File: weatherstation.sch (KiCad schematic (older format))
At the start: 29 parts, among them J1 Conn_02x13_Odd_Even, J10 Conn_01x03_Male, J2 Conn_01x02_Male, J3 Conn_01x02_Male, J4 Conn_01x02_Male, J5 Conn_01x02_Male, J6 Conn_01x02_Male, J7 Conn_01x02_Male, J8 Conn_01x02_Male, J9 Conn_01x02_Male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

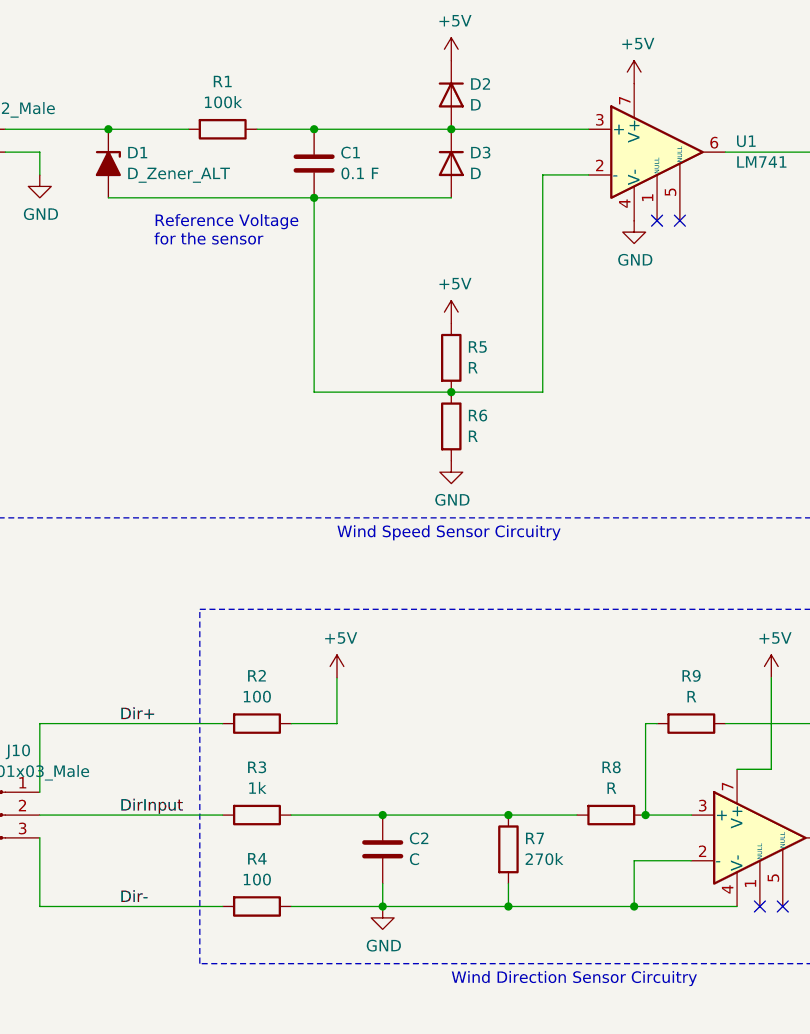
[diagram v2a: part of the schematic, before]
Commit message: Added footprints to schematic and generated netlist
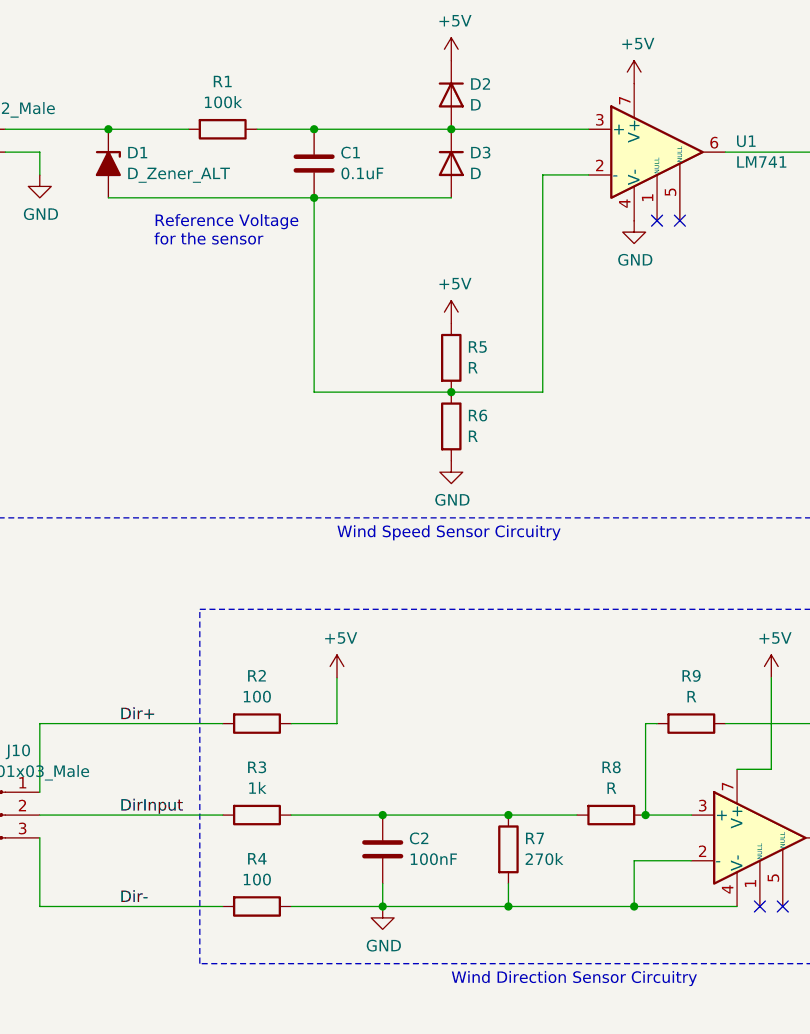
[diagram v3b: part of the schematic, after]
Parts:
- C1: value 0.1 F -> 0.1uF; footprint (none) -> Capacitor_THT:CP_Radial_D5.0mm_P2.50mm
- C2: value C -> 100nF; footprint (none) -> Capacitor_THT:C_Rect_L4.0mm_W2.5mm_P2.50mm
- D1, D2, D3: footprint (none) -> Diode_THT:D_A-405_P7.62mm_Horizontal
- D4: footprint (none) -> LED_THT:LED_D5.0mm
- J1: footprint (none) -> Connector_PinHeader_2.54mm:PinHeader_2x13_P2.54mm_Vertical
- J10: footprint (none) -> Connector_PinHeader_2.54mm:PinHeader_1x03_P2.54mm_Vertical
- J2, J3, J4, J5, J6, J7, J8, J9: footprint (none) -> Connector_PinHeader_2.54mm:PinHeader_1x02_P2.54mm_Vertical
- R1, R10, R2, R3, R4, R5, R6, R7, R8, R9: footprint (none) -> Resistor_THT:R_Axial_DIN0207_L6.3mm_D2.5mm_P10.16mm_Horizontal
- U1, U2: footprint (none) -> Package_DIP:DIP-8_W7.62mm
- U3: footprint (none) -> Package_DIP:DIP-16_W7.62mm
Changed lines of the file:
@@
 $EndDescr
-$Comp
-L Device:C C1
-U 1 1 60C0C43B
-P 2450 1350
-F 0 "C1" H 2565 1396 50  0000 L CNN
-F 1 "0.1 F" H 2565 1305 50  0000 L CNN
-F 2 "" H 2488 1200 50  0001 C CNN
-F 3 "~" H 2450 1350 50  0001 C CNN
-	1    2450 1350
-	1    0    0    -1
-$EndComp
-$Comp
-L Device:R R1
-U 1 1 60C0D3DD
-P 2050 1200
-F 0 "R1" V 1843 1200 50  0000 C CNN
-F 1 "100k" V 1934 1200 50  0000 C CNN
-F 2 "" V 1980 1200 50  0001 C CNN
-F 3 "~" H 2050 1200 50  0001 C CNN
-	1    2050 1200
-	0    1    1    0
-$EndComp
-Wire Wire Line
-	2200 1200 2450 1200
 $Comp
 L Device:D_Zener_ALT D1
@@
 F 0 "D1" V 1504 1430 50  0000 L CNN
 F 1 "D_Zener_ALT" V 1595 1430 50  0000 L CNN
-F 2 "" H 1550 1350 50  0001 C CNN
+F 2 "Diode_THT:D_A-405_P7.62mm_Horizontal" H 1550 1350 50  0001 C CNN
 F 3 "~" H 1550 1350 50  0001 C CNN
 	1    1550 1350
 	0    1    1    0
 $EndComp
-Wire Wire Line
-	1900 1200 1550 1200
 $Comp
 L Device:D D3
@@
 F 0 "D3" V 3004 1430 50  0000 L CNN
 F 1 "D" V 3095 1430 50  0000 L CNN
-F 2 "" H 3050 1350 50  0001 C CNN
+F 2 "Diode_THT:D_A-405_P7.62mm_Horizontal" H 3050 1350 50  0001 C CNN
 F 3 "~" H 3050 1350 50  0001 C CNN
 	1    3050 1350
@@
 F 0 "D2" V 3004 1130 50  0000 L CNN
 F 1 "D" V 3095 1130 50  0000 L CNN
-F 2 "" H 3050 1050 50  0001 C CNN
+F 2 "Diode_THT:D_A-405_P7.62mm_Horizontal" H 3050 1050 50  0001 C CNN
 F 3 "~" H 3050 1050 50  0001 C CNN
 	1    3050 1050
 	0    1    1    0
 $EndComp
-Wire Wire Line
-	2450 1200 3050 1200
-Connection ~ 2450 1200
 Connection ~ 3050 1200
 $Comp
@@
 F 0 "U1" H 4294 1346 50  0000 L CNN
 F 1 "LM741" H 4294 1255 50  0000 L CNN
-F 2 "" H 4000 1350 50  0001 C CNN
+F 2 "Package_DIP:DIP-8_W7.62mm" H 4000 1350 50  0001 C CNN
 F 3 "http://www.ti.com/lit/ds/symlink/lm741.pdf" H 4100 1450 50  0001 C CNN
 	1    3950 1300
@@
 F 0 "R5" H 3120 2246 50  0000 L CNN
 F 1 "R" H 3120 2155 50  0000 L CNN
-F 2 "" V 2980 2200 50  0001 C CNN
+F 2 "Resistor_THT:R_Axial_DIN0207_L6.3mm_D2.5mm_P10.16mm_Horizontal" V 2980 2200 50  0001 C CNN
 F 3 "~" H 3050 2200 50  0001 C CNN
 	1    3050 2200
@@
 F 0 "R6" H 3120 2546 50  0000 L CNN
 F 1 "R" H 3120 2455 50  0000 L CNN
-F 2 "" V 2980 2500 50  0001 C CNN
+F 2 "Resistor_THT:R_Axial_DIN0207_L6.3mm_D2.5mm_P10.16mm_Horizontal" V 2980 2500 50  0001 C CNN
 F 3 "~" H 3050 2500 50  0001 C CNN
 	1    3050 2500
@@
 F 0 "R10" H 4770 1496 50  0000 L CNN
 F 1 "R" H 4770 1405 50  0000 L CNN
-F 2 "" V 4630 1450 50  0001 C CNN
+F 2 "Resistor_THT:R_Axial_DIN0207_L6.3mm_D2.5mm_P10.16mm_Horizontal" V 4630 1450 50  0001 C CNN
 F 3 "~" H 4700 1450 50  0001 C CNN
 	1    4700 1450
@@
 F 0 "D4" V 4739 1632 50  0000 R CNN
 F 1 "LED" V 4648 1632 50  0000 R CNN
-F 2 "" H 4700 1750 50  0001 C CNN
+F 2 "LED_THT:LED_D5.0mm" H 4700 1750 50  0001 C CNN
 F 3 "~" H 4700 1750 50  0001 C CNN
 	1    4700 1750
@@
 F 0 "U3" H 6550 2431 50  0000 C CNN
 F 1 "MCP3008" H 6550 2340 50  0000 C CNN
-F 2 "" H 6650 1850 50  0001 C CNN
+F 2 "Package_DIP:DIP-16_W7.62mm" H 6650 1850 50  0001 C CNN
 F 3 "http://ww1.microchip.com/downloads/en/DeviceDoc/21295d.pdf" H 6650 1850 50  0001 C CNN
 	1    6550 1750
@@
 F 0 "R9" V 3893 3800 50  0000 C CNN
 F 1 "R" V 3984 3800 50  0000 C CNN
-F 2 "" V 4030 3800 50  0001 C CNN
+F 2 "Resistor_THT:R_Axial_DIN0207_L6.3mm_D2.5mm_P10.16mm_Horizontal" V 4030 3800 50  0001 C CNN
 F 3 "~" H 4100 3800 50  0001 C CNN
 	1    4100 3800
@@
 F 0 "R8" V 3543 4200 50  0000 C CNN
 F 1 "R" V 3634 4200 50  0000 C CNN
-F 2 "" V 3680 4200 50  0001 C CNN
+F 2 "Resistor_THT:R_Axial_DIN0207_L6.3mm_D2.5mm_P10.16mm_Horizontal" V 3680 4200 50  0001 C CNN
 F 3 "~" H 3750 4200 50  0001 C CNN
 	1    3750 4200
@@
 F 0 "U2" H 4744 4346 50  0000 L CNN
 F 1 "LM741" H 4744 4255 50  0000 L CNN
-F 2 "" H 4450 4350 50  0001 C CNN
+F 2 "Package_DIP:DIP-8_W7.62mm" H 4450 4350 50  0001 C CNN
 F 3 "http://www.ti.com/lit/ds/symlink/lm741.pdf" H 4550 4450 50  0001 C CNN
 	1    4400 4300
@@
 F 0 "R7" H 3370 4396 50  0000 L CNN
 F 1 "270k" H 3370 4305 50  0000 L CNN
-F 2 "" V 3230 4350 50  0001 C CNN
+F 2 "Resistor_THT:R_Axial_DIN0207_L6.3mm_D2.5mm_P10.16mm_Horizontal" V 3230 4350 50  0001 C CNN
 F 3 "~" H 3300 4350 50  0001 C CNN
 	1    3300 4350
@@
 P 2750 4350
 F 0 "C2" H 2865 4396 50  0000 L CNN
-F 1 "C" H 2865 4305 50  0000 L CNN
-F 2 "" H 2788 4200 50  0001 C CNN
+F 1 "100nF" H 2865 4305 50  0000 L CNN
+F 2 "Capacitor_THT:C_Rect_L4.0mm_W2.5mm_P2.50mm" H 2788 4200 50  0001 C CNN
 F 3 "~" H 2750 4350 50  0001 C CNN
 	1    2750 4350
@@
 F 0 "R3" V 1993 4200 50  0000 C CNN
 F 1 "1k" V 2084 4200 50  0000 C CNN
-F 2 "" V 2130 4200 50  0001 C CNN
+F 2 "Resistor_THT:R_Axial_DIN0207_L6.3mm_D2.5mm_P10.16mm_Horizontal" V 2130 4200 50  0001 C CNN
 F 3 "~" H 2200 4200 50  0001 C CNN
 	1    2200 4200
@@
 F 0 "R4" V 1993 4600 50  0000 C CNN
 F 1 "100" V 2084 4600 50  0000 C CNN
-F 2 "" V 2130 4600 50  0001 C CNN
+F 2 "Resistor_THT:R_Axial_DIN0207_L6.3mm_D2.5mm_P10.16mm_Horizontal" V 2130 4600 50  0001 C CNN
 F 3 "~" H 2200 4600 50  0001 C CNN
 	1    2200 4600
@@
 F 0 "R2" V 1993 3800 50  0000 C CNN
 F 1 "100" V 2084 3800 50  0000 C CNN
-F 2 "" V 2130 3800 50  0001 C CNN
+F 2 "Resistor_THT:R_Axial_DIN0207_L6.3mm_D2.5mm_P10.16mm_Horizontal" V 2130 3800 50  0001 C CNN
 F 3 "~" H 2200 3800 50  0001 C CNN
 	1    2200 3800
@@
 F 0 "J6" H 9308 4831 50  0000 C CNN
 F 1 "Conn_01x02_Male" H 9308 4740 50  0000 C CNN
-F 2 "" H 9200 4650 50  0001 C CNN
+F 2 "Connector_PinHeader_2.54mm:PinHeader_1x02_P2.54mm_Vertical" H 9200 4650 50  0001 C CNN
 F 3 "~" H 9200 4650 50  0001 C CNN
 	1    9200 4650
@@
 F 0 "J7" H 9308 5281 50  0000 C CNN
 F 1 "Conn_01x02_Male" H 9308 5190 50  0000 C CNN
-F 2 "" H 9200 5100 50  0001 C CNN
+F 2 "Connector_PinHeader_2.54mm:PinHeader_1x02_P2.54mm_Vertical" H 9200 5100 50  0001 C CNN
 F 3 "~" H 9200 5100 50  0001 C CNN
 	1    9200 5100
@@
 F 0 "J8" H 9308 5681 50  0000 C CNN
 F 1 "Conn_01x02_Male" H 9308 5590 50  0000 C CNN
-F 2 "" H 9200 5500 50  0001 C CNN
+F 2 "Connector_PinHeader_2.54mm:PinHeader_1x02_P2.54mm_Vertical" H 9200 5500 50  0001 C CNN
 F 3 "~" H 9200 5500 50  0001 C CNN
 	1    9200 5500
@@
 F 0 "J9" H 9308 6081 50  0000 C CNN
 F 1 "Conn_01x02_Male" H 9308 5990 50  0000 C CNN
-F 2 "" H 9200 5900 50  0001 C CNN
+F 2 "Connector_PinHeader_2.54mm:PinHeader_1x02_P2.54mm_Vertical" H 9200 5900 50  0001 C CNN
 F 3 "~" H 9200 5900 50  0001 C CNN
 	1    9200 5900
@@
 F 0 "J5" H 9308 4431 50  0000 C CNN
 F 1 "Conn_01x02_Male" H 9308 4340 50  0000 C CNN
-F 2 "" H 9200 4250 50  0001 C CNN
+F 2 "Connector_PinHeader_2.54mm:PinHeader_1x02_P2.54mm_Vertical" H 9200 4250 50  0001 C CNN
 F 3 "~" H 9200 4250 50  0001 C CNN
 	1    9200 4250
@@
 F 0 "J4" H 9308 4031 50  0000 C CNN
 F 1 "Conn_01x02_Male" H 9308 3940 50  0000 C CNN
-F 2 "" H 9200 3850 50  0001 C CNN
+F 2 "Connector_PinHeader_2.54mm:PinHeader_1x02_P2.54mm_Vertical" H 9200 3850 50  0001 C CNN
 F 3 "~" H 9200 3850 50  0001 C CNN
 	1    9200 3850
@@
 F 0 "J3" H 9308 3631 50  0000 C CNN
 F 1 "Conn_01x02_Male" H 9308 3540 50  0000 C CNN
-F 2 "" H 9200 3450 50  0001 C CNN
+F 2 "Connector_PinHeader_2.54mm:PinHeader_1x02_P2.54mm_Vertical" H 9200 3450 50  0001 C CNN
 F 3 "~" H 9200 3450 50  0001 C CNN
 	1    9200 3450
@@
 F 0 "J2" H 1008 1381 50  0000 C CNN
 F 1 "Conn_01x02_Male" H 1008 1290 50  0000 C CNN
-F 2 "" H 900 1200 50  0001 C CNN
+F 2 "Connector_PinHeader_2.54mm:PinHeader_1x02_P2.54mm_Vertical" H 900 1200 50  0001 C CNN
 F 3 "~" H 900 1200 50  0001 C CNN
 	1    900  1200
@@
 Wire Wire Line
 	1100 1200 1550 1200
-Connection ~ 1550 1200
 $Comp
 L power:GND #PWR0116
@@
 F 0 "J1" H 9100 2617 50  0000 C CNN
 F 1 "Conn_02x13_Odd_Even" H 9100 2526 50  0000 C CNN
-F 2 "" H 9050 1800 50  0001 C CNN
+F 2 "Connector_PinHeader_2.54mm:PinHeader_2x13_P2.54mm_Vertical" H 9050 1800 50  0001 C CNN
 F 3 "~" H 9050 1800 50  0001 C CNN
 	1    9050 1800
@@
 F 0 "J10" H 1158 4481 50  0000 C CNN
 F 1 "Conn_01x03_Male" H 1158 4390 50  0000 C CNN
-F 2 "" H 1050 4200 50  0001 C CNN
+F 2 "Connector_PinHeader_2.54mm:PinHeader_1x03_P2.54mm_Vertical" H 1050 4200 50  0001 C CNN
 F 3 "~" H 1050 4200 50  0001 C CNN
 	1    1050 4200
@@
 Wire Wire Line
 	1250 4600 2050 4600
+Connection ~ 2450 1200
+Wire Wire Line
+	2450 1200 3050 1200
+Wire Wire Line
+	2200 1200 2450 1200
+$Comp
+L Device:R R1
+U 1 1 60C0D3DD
+P 2050 1200
+F 0 "R1" V 1843 1200 50  0000 C CNN
+F 1 "100k" V 1934 1200 50  0000 C CNN
+F 2 "Resistor_THT:R_Axial_DIN0207_L6.3mm_D2.5mm_P10.16mm_Horizontal" V 1980 1200 50  0001 C CNN
+F 3 "~" H 2050 1200 50  0001 C CNN
+	1    2050 1200
+	0    1    1    0
+$EndComp
+$Comp
+L Device:C C1
+U 1 1 60C0C43B
+P 2450 1350
+F 0 "C1" H 2565 1396 50  0000 L CNN
+F 1 "0.1uF" H 2565 1305 50  0000 L CNN
+F 2 "Capacitor_THT:CP_Radial_D5.0mm_P2.50mm" H 2488 1200 50  0001 C CNN
+F 3 "~" H 2450 1350 50  0001 C CNN
+	1    2450 1350
+	1    0    0    -1
+$EndComp
+Connection ~ 1550 1200
+Wire Wire Line
+	1900 1200 1550 1200
 $EndSCHEMATC

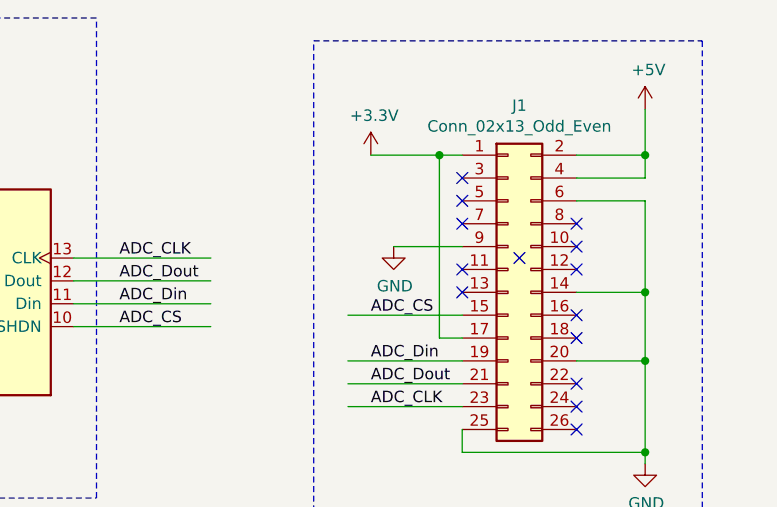
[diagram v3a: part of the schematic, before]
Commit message: Fixed backwards raspi header
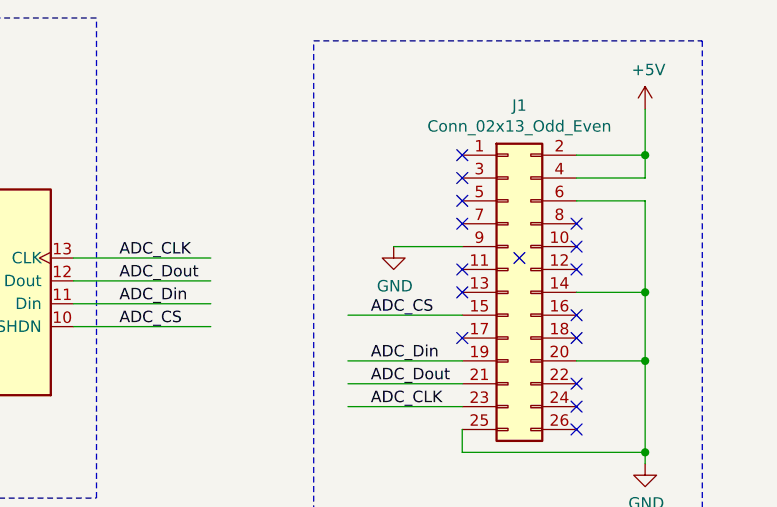
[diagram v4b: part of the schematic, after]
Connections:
- net labels removed: +3.3V
- wire segments 104 -> 100
- no-connect marks 18 -> 20
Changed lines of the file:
@@
 	1    0    0    -1
 $EndComp
-$Comp
-L power:+3.3V #PWR0107
-U 1 1 61007AFD
-P 8450 1200
-F 0 "#PWR0107" H 8450 1050 50  0001 C CNN
-F 1 "+3.3V" H 8465 1373 50  0000 C CNN
-F 2 "" H 8450 1200 50  0001 C CNN
-F 3 "" H 8450 1200 50  0001 C CNN
-	1    8450 1200
-	1    0    0    -1
-$EndComp
-Wire Wire Line
-	8450 1200 8750 1200
 Text Label 8450 2200 0    50   ~ 0
 ADC_Dout
@@
 Wire Wire Line
 	9650 2100 9650 2500
-Wire Wire Line
-	8850 2000 8750 2000
-Wire Wire Line
-	8750 2000 8750 1200
-Connection ~ 8750 1200
-Wire Wire Line
-	8750 1200 8850 1200
 Wire Wire Line
 	8850 2400 8850 2500
@@
 Wire Wire Line
 	1900 1200 1550 1200
+NoConn ~ 8850 2000
+NoConn ~ 8850 1200
 $EndSCHEMATC
